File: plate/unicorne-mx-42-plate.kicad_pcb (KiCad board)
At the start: 2 copper layers, 299.9 x 118.8 mm, 12 parts

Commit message: Solid 42- and 36-key switch plates for MX and Choc; re-export everything
Plates no longer have break lines. Each switch type gets a 42-key plate and a
36-key plate cut where the PCB snaps off its outer columns, with rounded
corners and only the holes whose screw head fits. PCB gerbers, STEP and
renders regenerated.

Co-Authored-By: Claude Opus 5.5 <noreply@anthropic.com>
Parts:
- removed MB1, MB2: mouse bites, 
- moved H6 8.05 mm to (269.7, 95.2)
- moved H1 2.57 mm to (134.3, 72.6)
- moved H5 2.02 mm to (225.7, 72.6)
- moved H4 1.80 mm to (78.0, 59.8)
- moved H2 1.52 mm to (97.0, 101.5)
- moved H8 1.25 mm to (282.0, 59.8)
- moved H3 0.50 mm to (134.4, 121.6)
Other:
- outline, holes or cut-outs redrawn
- board text added: "unicorne MX 42"
- board text removed: "unicorne CHOC plate"

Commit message: Halves closer, trackpad on the case; GND repair in the router; re-export
- The trackpad sits on the case above the board, so it may cover the
  nice!nano. layout.py places it where its keycap keep-out lets the halves
  come closest: each half moves 3.25 mm inward and the board is 293.4 mm wide
  (was 299.9). The parts below it follow; it has no 3D model on the board.
- The level shifter group (U2, C2, JP3) moves down, clear of the inner
  column, which now comes within ~6.5 mm of the headers.
- J3/J4 headers have no 3D model (bare holes in the renders and STEP).
- finish_route.py: jitters the routing order between attempts, and repairs
  GND the pours left cut off (tools/gnd_repair.py: a via where the pocket
  overlaps the main ground, else rip up the net boxing it in and reroute).
- Both boards rerouted: DRC 0 unconnected, schematic parity 0, every pin,
  the matrix, the LED chain and one GND group verified. Gerbers, STEP,
  renders and all four plates regenerated. copper_sliver (a thin point in a
  GND pour) counts as harmless for the gerber export.

Co-Authored-By: Claude Opus 5.5 <noreply@anthropic.com>
Claude-Session: https://claude.ai/code/session_01D39ubfTYtq6FMvNmmbStTo
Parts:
- moved H5 6.25 mm to (219.5, 72.6)
- moved H6 6.25 mm to (263.5, 95.2)
- moved H7 6.25 mm to (219.3, 121.6)
- moved H8 6.25 mm to (275.8, 59.8)
- moved H10 3.59 mm to (191.0, 131.6)
- moved H9 3.59 mm to (163.0, 131.6)
- moved H1 0.25 mm to (134.5, 72.6)
- moved H2 0.25 mm to (97.3, 101.5)
- moved H3 0.25 mm to (134.7, 121.6)
- moved H4 0.25 mm to (78.2, 59.8)
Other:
- board size 299.9 x 118.8 mm -> 293.4 x 118.8 mm

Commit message: Plates: openings for the nice!nano (through the top edge) and the reset switch
Both from where the PCB has them, 0.5 mm clearance, 0.8 mm corner radius. The
nano opening joins the trackpad opening; all four plates pass DRC.

Co-Authored-By: Claude Opus 5.5 <noreply@anthropic.com>
Claude-Session: https://claude.ai/code/session_01D39ubfTYtq6FMvNmmbStTo
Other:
- outline, holes or cut-outs redrawn

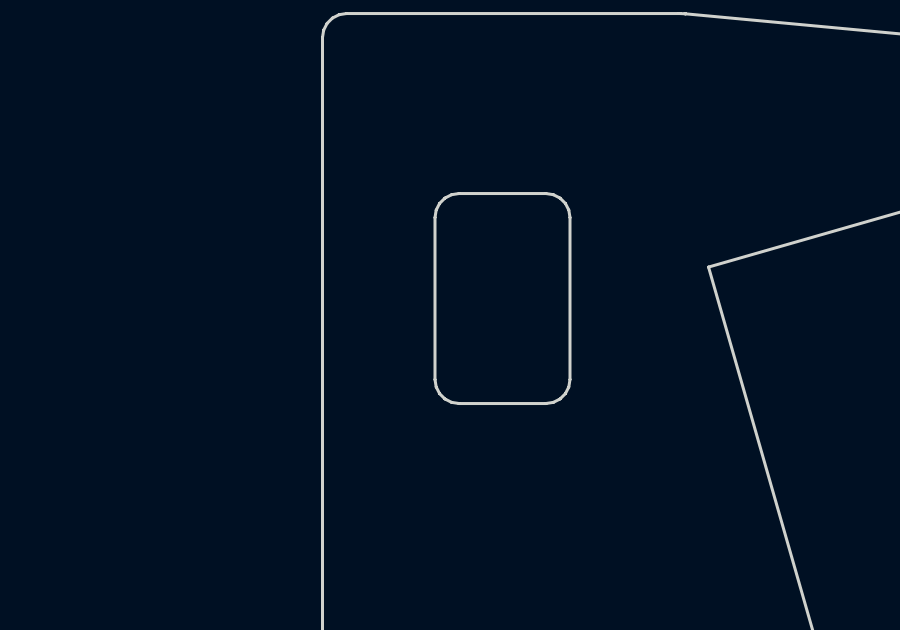
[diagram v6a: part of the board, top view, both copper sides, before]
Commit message: Add Linux KiCad path support, host tests and setup notes
Co-Authored-By: Claude Opus 5 <noreply@anthropic.com>
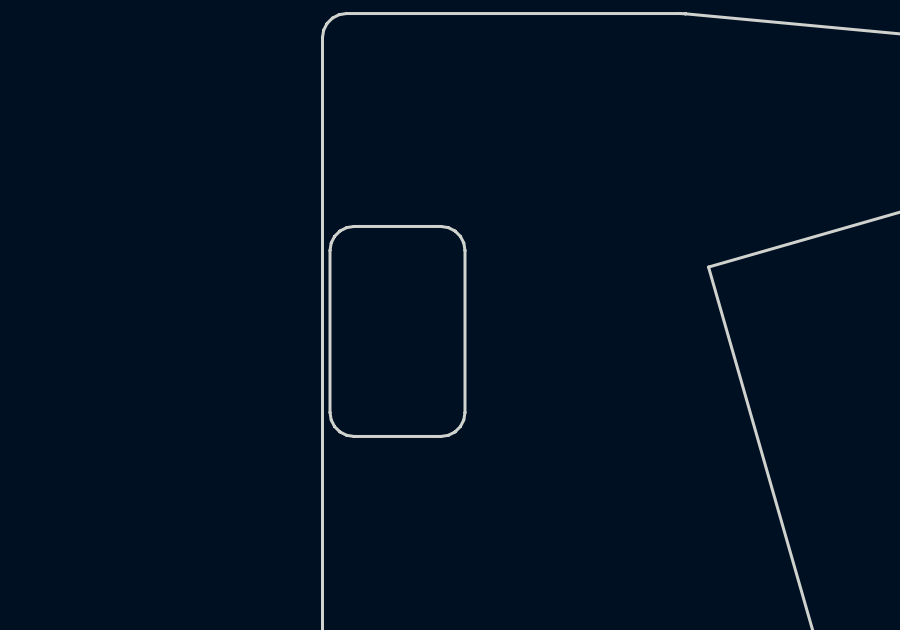
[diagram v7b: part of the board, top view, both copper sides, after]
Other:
- outline, holes or cut-outs redrawn
